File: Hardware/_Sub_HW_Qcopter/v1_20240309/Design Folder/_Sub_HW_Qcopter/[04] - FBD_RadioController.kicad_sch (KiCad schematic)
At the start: 0 parts

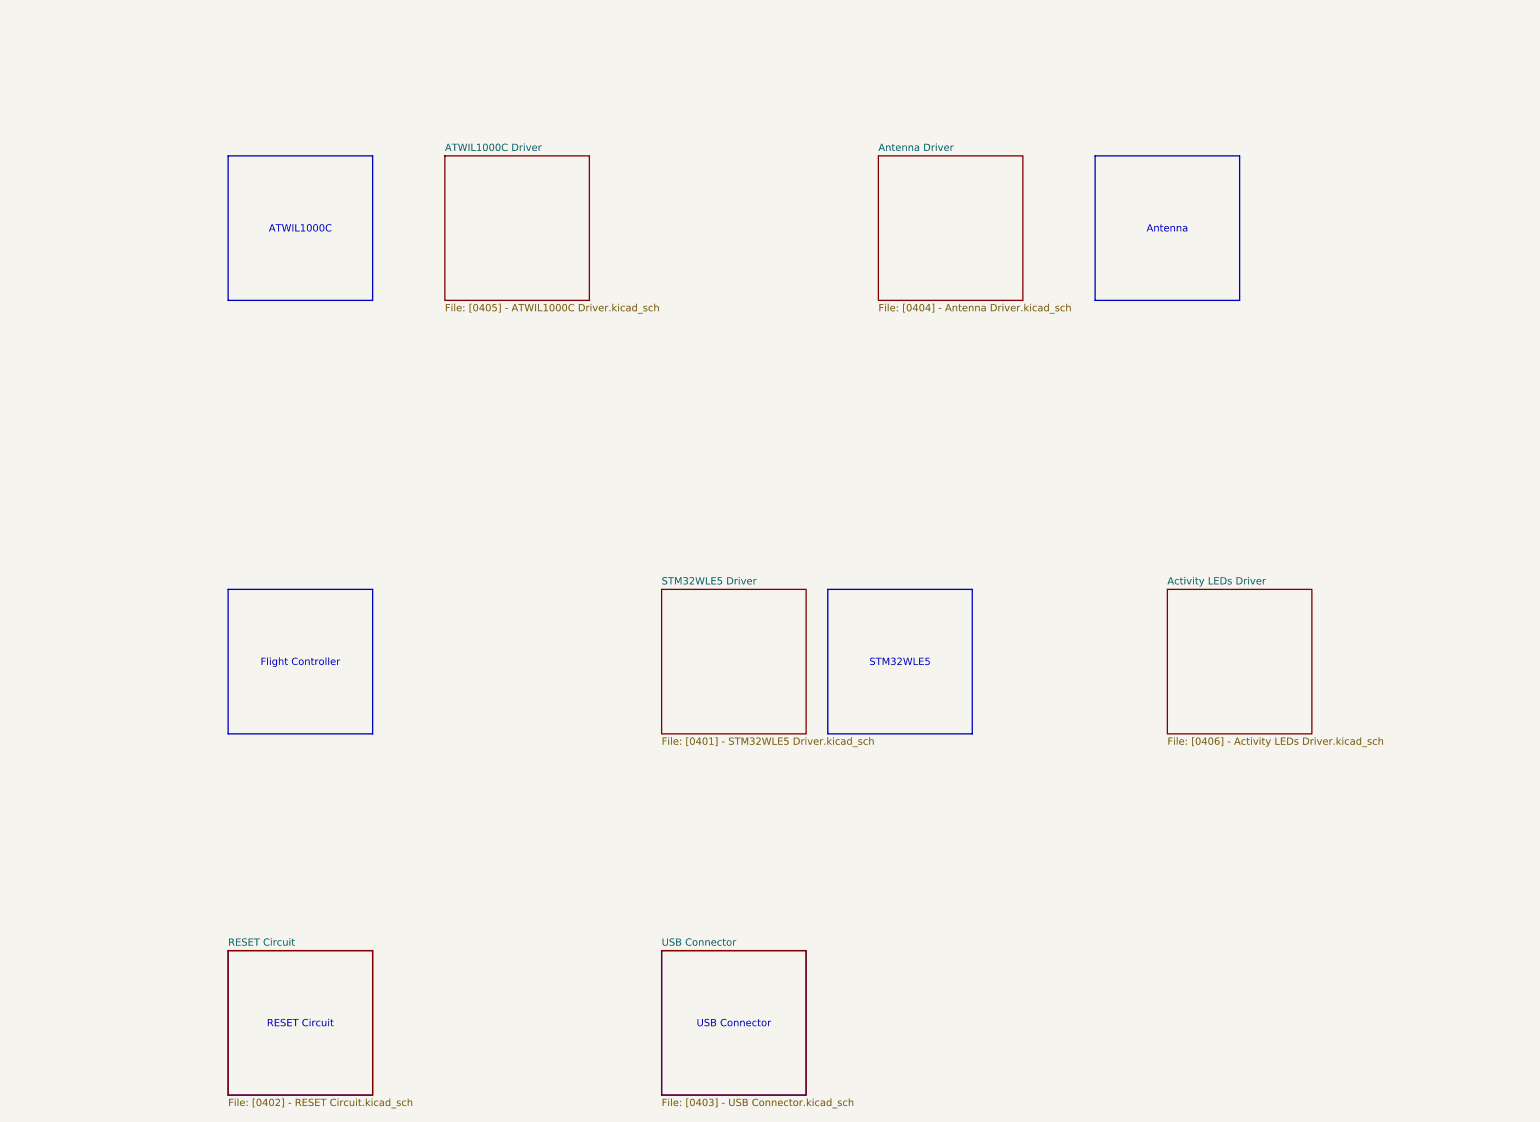
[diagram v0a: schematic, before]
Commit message: Schematic is done by 90%
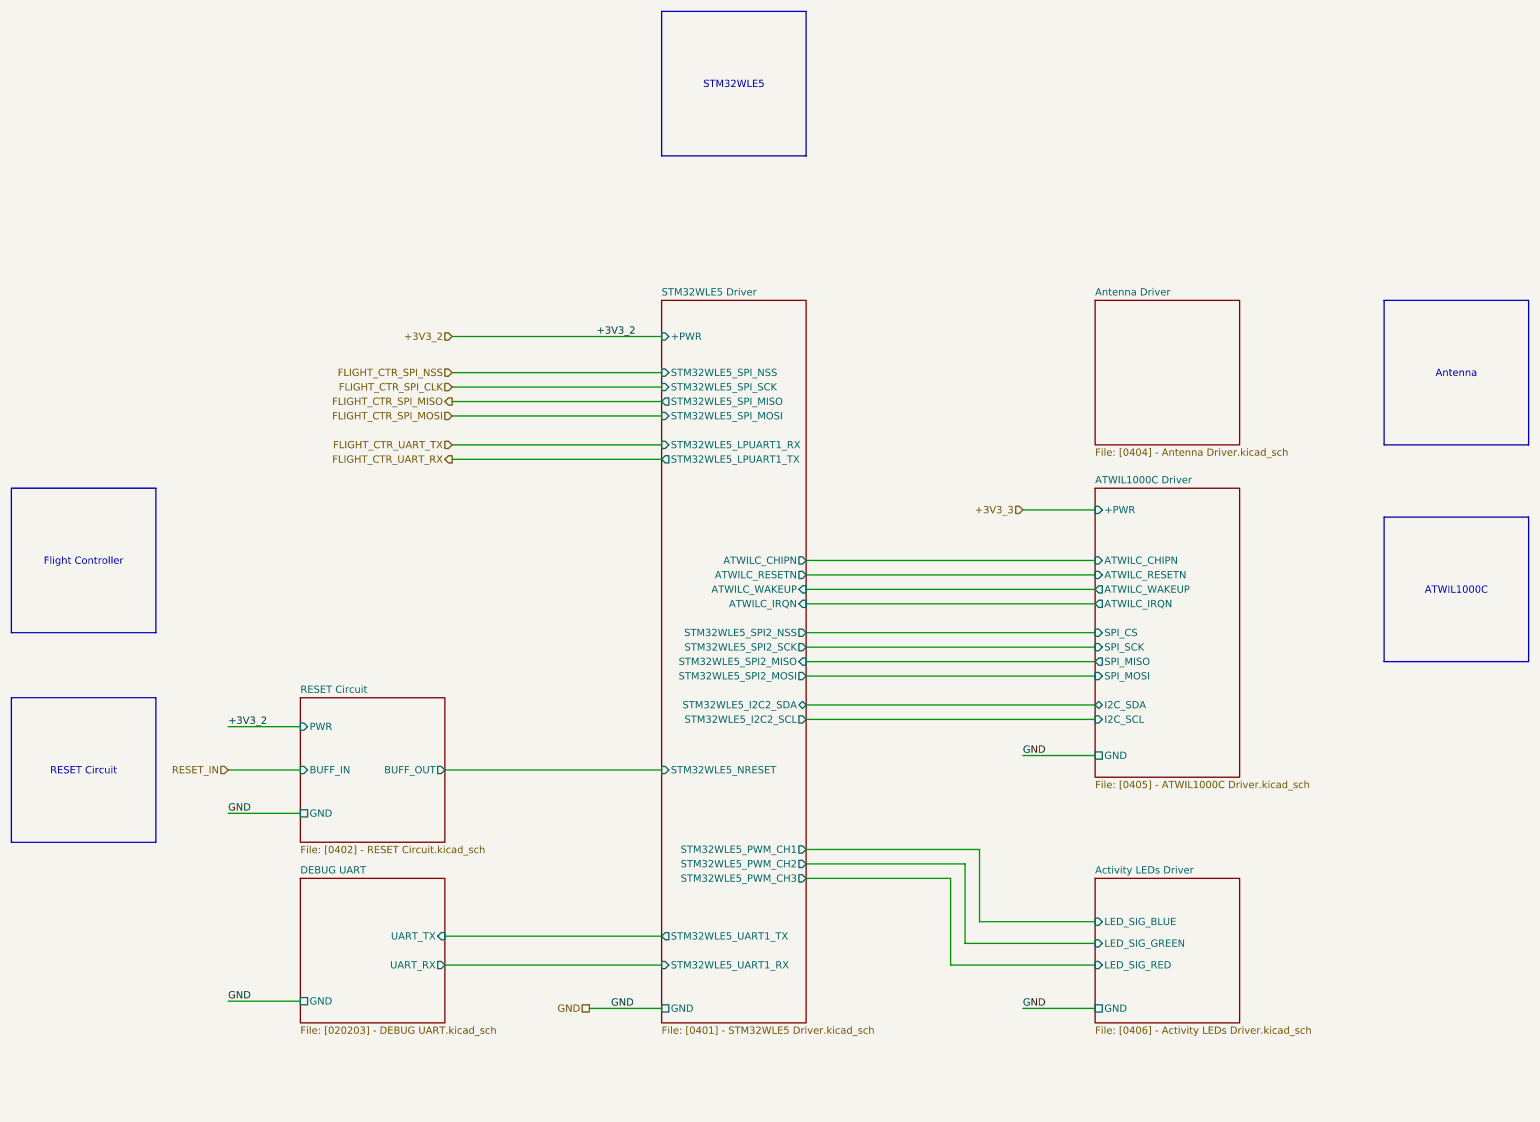
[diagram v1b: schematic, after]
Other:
- removed sheet USB Connector
- added sheet DEBUG UART ([020203] - DEBUG UART.kicad_sch)
- sheet ATWIL1000C Driver ports: added +PWR, ATWILC_CHIPN, ATWILC_IRQN, ATWILC_RESETN, ATWILC_WAKEUP, GND, I2C_SCL, I2C_SDA, SPI_CS, SPI_MISO, SPI_MOSI, SPI_SCK; removed none
- sheet Activity LEDs Driver ports: added GND, LED_SIG_BLUE, LED_SIG_GREEN, LED_SIG_RED; removed none
- sheet RESET Circuit ports: added BUFF_IN, BUFF_OUT, GND, PWR; removed none
- sheet STM32WLE5 Driver ports: added +PWR, ATWILC_CHIPN, ATWILC_IRQN, ATWILC_RESETN, ATWILC_WAKEUP, GND, STM32WLE5_I2C2_SCL, STM32WLE5_I2C2_SDA, STM32WLE5_LPUART1_RX, STM32WLE5_LPUART1_TX, STM32WLE5_NRESET, STM32WLE5_PWM_CH1, STM32WLE5_PWM_CH2, STM32WLE5_PWM_CH3, STM32WLE5_SPI2_MISO, STM32WLE5_SPI2_MOSI, STM32WLE5_SPI2_NSS, STM32WLE5_SPI2_SCK, STM32WLE5_SPI_MISO, STM32WLE5_SPI_MOSI, STM32WLE5_SPI_NSS, STM32WLE5_SPI_SCK, STM32WLE5_UART1_RX, STM32WLE5_UART1_TX; removed none

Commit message: 97% drawing schematic is done
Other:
- sheet ATWIL1000C Driver ports: added +PWR_+3.3V; removed +PWR
- sheet Antenna Driver ports: added FE_CTRL1, FE_CTRL2, FE_CTRL3, RFI_N, RFI_P, RFO_HP, RFO_LP, VR_PA; removed none
- sheet STM32WLE5 Driver ports: added FE_CTRL1, FE_CTRL2, FE_CTRL3, STM32WLE5_RFIN, STM32WLE5_RFIP, STM32WLE5_RFOHP, STM32WLE5_RFOLP, STM32WLE5_VRPA; removed none
